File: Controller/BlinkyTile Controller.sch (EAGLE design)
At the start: 27 parts, among them CON1 USB_MICROSMT+THRUHULE, CON2 F-2X05-DIL-100, Q1 CRYSTAL_4PAD2520, SW1 SPST_TACT-EVQQ2, SW2 SPST_TACT-EVQQ2, U1 MK20D--VFM5, U2 W25Q80BV, U3 74LVC1G17DCK, U4 74LVC1G17DCK, U5 74LVC1G17DCK

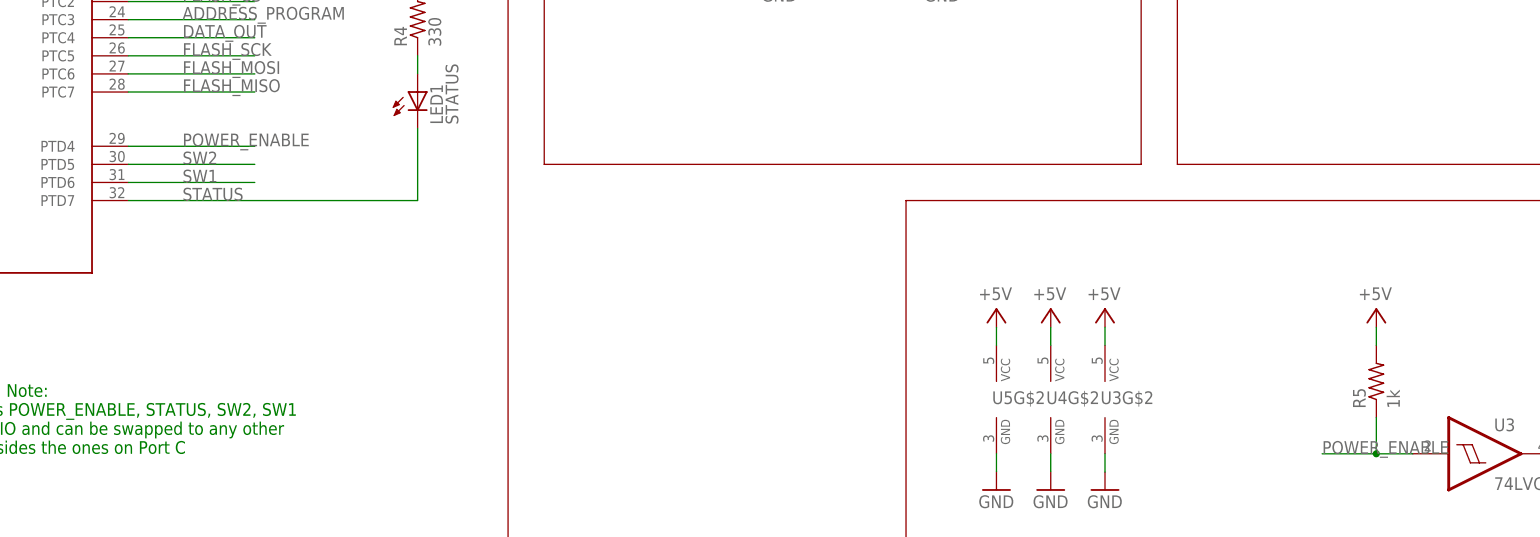
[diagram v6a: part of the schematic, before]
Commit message: Update controller: move R5 to 3.3v, reduce panel size, move more routing to top layer
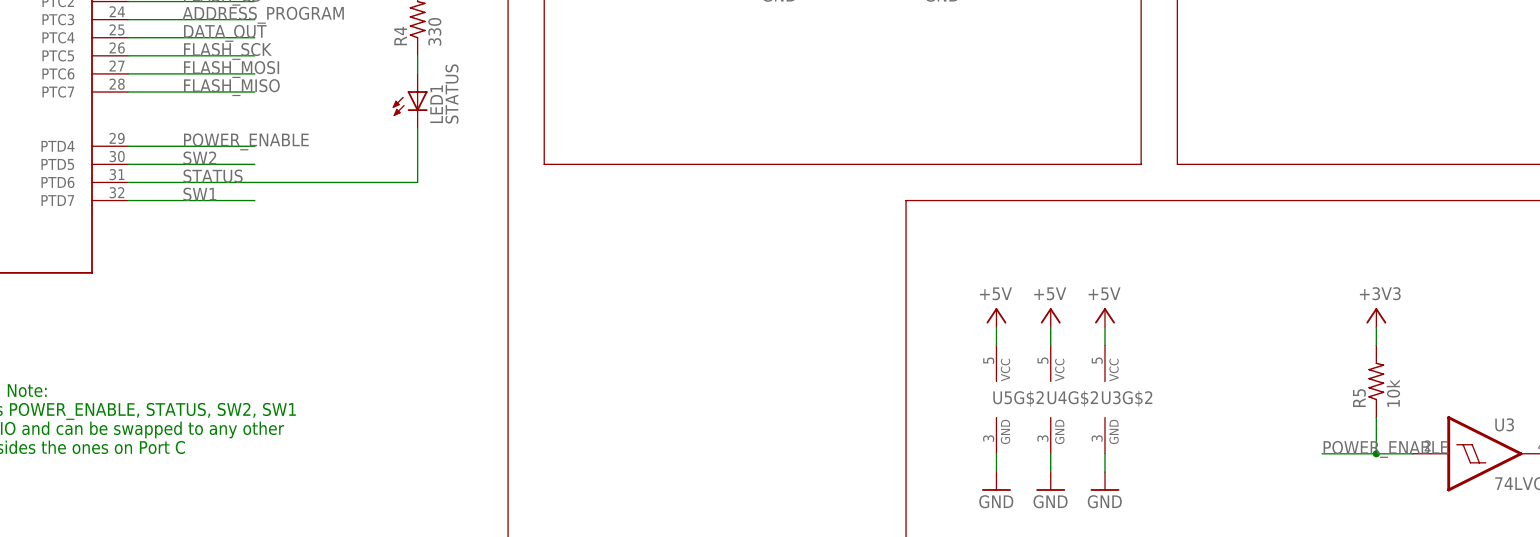
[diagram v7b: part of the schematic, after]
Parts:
- R5: value 1k -> 10k
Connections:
- net +3V3: now also R5.2
- net +5V: no longer R5.2
- net STATUS: now also U1.PTD6; no longer U1.PTD7
- net SW1: now also U1.PTD7; no longer U1.PTD6
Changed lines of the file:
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@@
 <part name="GND8" library="supply1" deviceset="GND" device=""/>
 <part name="C6" library="adafruit" deviceset="C-US" device="C0402" value="100nF"/>
-<part name="R5" library="adafruit" deviceset="R-US_" device="R0402" value="1k"/>
+<part name="R5" library="adafruit" deviceset="R-US_" device="R0402" value="10k"/>
 <part name="SV1" library="dodocohedreled" deviceset="4-PIN_DUPONT" device=""/>
-<part name="P+5" library="supply1" deviceset="+5V" device=""/>
 <part name="C8" library="adafruit" deviceset="C-US" device="C0805K" value="10uF"/>
 <part name="GND11" library="supply1" deviceset="GND" device=""/>
+<part name="3V4" library="supply1" deviceset="+3V3" device=""/>
 </parts>
 <sheets>
@@
 <instance part="R5" gate="G$1" x="322.58" y="134.62" rot="R90"/>
 <instance part="SV1" gate="1" x="373.38" y="101.6" rot="R180"/>
-<instance part="P+5" gate="1" x="322.58" y="144.78" smashed="yes">
-<attribute name="VALUE" x="320.04" y="146.05" size="1.778" layer="96"/>
-</instance>
 <instance part="C8" gate="G$1" x="78.74" y="213.36"/>
 <instance part="GND11" gate="1" x="78.74" y="203.2"/>
+<instance part="3V4" gate="G$1" x="322.58" y="144.78" smashed="yes">
+<attribute name="VALUE" x="320.04" y="146.05" size="1.778" layer="96"/>
+</instance>
 </instances>
 <busses>
@@
 <pinref part="U3" gate="G$2" pin="VCC"/>
 <wire x1="284.48" y1="142.24" x2="284.48" y2="139.7" width="0.1524" layer="91"/>
-</segment>
-<segment>
-<pinref part="R5" gate="G$1" pin="2"/>
-<wire x1="322.58" y1="142.24" x2="322.58" y2="139.7" width="0.1524" layer="91"/>
-<pinref part="P+5" gate="1" pin="+5V"/>
 </segment>
 </net>
@@
 <label x="27.94" y="137.16" size="1.778" layer="95"/>
 </segment>
+<segment>
+<pinref part="R5" gate="G$1" pin="2"/>
+<pinref part="3V4" gate="G$1" pin="+3V3"/>
+<wire x1="322.58" y1="142.24" x2="322.58" y2="139.7" width="0.1524" layer="91"/>
+</segment>
 </net>
 <net name="TCLK" class="0">
@@
 <segment>
 <pinref part="LED1" gate="G$1" pin="C"/>
-<wire x1="187.96" y1="170.18" x2="187.96" y2="160.02" width="0.1524" layer="91"/>
-<pinref part="U1" gate="G$1" pin="PTD7"/>
-<wire x1="147.32" y1="160.02" x2="187.96" y2="160.02" width="0.1524" layer="91"/>
-<label x="154.94" y="160.02" size="1.778" layer="95"/>
+<wire x1="187.96" y1="170.18" x2="187.96" y2="162.56" width="0.1524" layer="91"/>
+<pinref part="U1" gate="G$1" pin="PTD6"/>
+<wire x1="147.32" y1="162.56" x2="187.96" y2="162.56" width="0.1524" layer="91"/>
+<label x="154.94" y="162.56" size="1.778" layer="95"/>
 </segment>
 </net>
@@
 </segment>
 <segment>
-<pinref part="U1" gate="G$1" pin="PTD6"/>
-<wire x1="147.32" y1="162.56" x2="165.1" y2="162.56" width="0.1524" layer="91"/>
-<label x="154.94" y="162.56" size="1.778" layer="95"/>
+<pinref part="U1" gate="G$1" pin="PTD7"/>
+<wire x1="147.32" y1="160.02" x2="165.1" y2="160.02" width="0.1524" layer="91"/>
+<label x="154.94" y="160.02" size="1.778" layer="95"/>
 </segment>
 </net>
@@
 </sheet>
 </sheets>
+<errors>
+</errors>
 </schematic>
 </drawing>
